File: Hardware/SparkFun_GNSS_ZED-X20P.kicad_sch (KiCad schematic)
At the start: 70 parts, among them J1 USB_C_Receptacle, J10 U.FL, J11 Conn_01x06, J2 Conn_01x06, J3 Conn_01x09, J4 Qwiic_RA, J5 SMA_Edge, J7 Qwiic_RA, J8 JST_Locking_4, J9 I2C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

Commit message: Add panel
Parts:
- added TP2: 1.0mm, SparkFun-Connector:TestPoint-1.0mm, symbol SparkFun-Connector:TestPoint_1.0mm
- L1, L2: value 33nH -> 47nH; symbol SparkFun-Coil:33nH_0603_0.3A -> SparkFun-Coil:47nH_0603_0.3A; Frequency 100MHz -> (none); PROD_ID NDUC-13805 -> NDUC-26402; Resistance (none) -> 0.72
- U5: symbol SparkFun-GPS:ZED-F9P -> SparkFun-GPS:ZED-X20P; PROD_ID IC-16923 -> IC-26061
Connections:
- net 3.3V: now also JP8.2 (B)
- net GEO_STAT: now also D9.1 (K); no longer JP8.2 (B)
- net GND: no longer D9.1 (K)
- net V_BCKP: now also TP2.1
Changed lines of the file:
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@@
 	(wire
 		(pts
+			(xy 260.35 156.21) (xy 260.35 157.48)
+		)
+		(stroke
+			(width 0)
+			(type default)
+		)
+	)
+	(wire
+		(pts
 			(xy 368.3 90.17) (xy 368.3 88.9)
 		)
@@
 		)
 	)
-	(global_label "GEO_STAT"
-		(shape output)
-		(at 269.24 218.44 90)
-		(fields_autoplaced yes)
-		(effects
-			(font
-				(size 1.27 1.27)
-			)
-			(justify left)
-		)
-		(property "Intersheetrefs" "${INTERSHEET_REFS}"
-			(at 269.24 207.1586 90)
-			(effects
-				(font
-					(size 1.27 1.27)
-				)
-				(justify left)
-				(hide yes)
-			)
-		)
-	)
 	(global_label "SDA{slash}~{CS}"
 		(shape bidirectional)
@@
 	)
 	(global_label "RF_IN"
-		(shape input)
+		(shape output)
 		(at 367.03 144.78 90)
 		(fields_autoplaced yes)
@@
 		)
 	)
+	(global_label "GEO_STAT"
+		(shape output)
+		(at 269.24 238.76 270)
+		(fields_autoplaced yes)
+		(effects
+			(font
+				(size 1.27 1.27)
+			)
+			(justify right)
+		)
+		(property "Intersheetrefs" "${INTERSHEET_REFS}"
+			(at 269.24 250.0414 90)
+			(effects
+				(font
+					(size 1.27 1.27)
+				)
+				(justify right)
+				(hide yes)
+			)
+		)
+	)
 	(global_label "RTK_STAT"
 		(shape output)
@@
 	)
 	(global_label "VCC_RF"
-		(shape output)
+		(shape input)
 		(at 389.89 163.83 0)
 		(fields_autoplaced yes)
@@
 	)
 	(symbol
-		(lib_id "SparkFun-Coil:33nH_0603_0.3A")
+		(lib_id "SparkFun-Connector:TestPoint_1.0mm")
+		(at 260.35 156.21 0)
+		(unit 1)
+		(exclude_from_sim no)
+		(in_bom yes)
+		(on_board yes)
+		(dnp no)
+		(fields_autoplaced yes)
+		(property "Reference" "TP2"
+			(at 260.35 151.13 0)
+			(do_not_autoplace yes)
+			(effects
+				(font
+					(size 1.27 1.27)
+				)
+			)
+		)
+		(property "Value" "1.0mm"
+			(at 260.35 160.02 0)
+			(effects
+				(font
+					(size 1.27 1.27)
+				)
+				(hide yes)
+			)
+		)
+		(property "Footprint" "SparkFun-Connector:TestPoint-1.0mm"
+			(at 260.35 162.56 0)
+			(effects
+				(font
+					(size 1.27 1.27)
+				)
+				(hide yes)
+			)
+		)
+		(property "Datasheet" "~"
+			(at 260.35 163.83 0)
+			(effects
+				(font
+					(size 1.27 1.27)
+				)
+				(hide yes)
+			)
+		)
+		(property "Description" "Test Point"
+			(at 260.35 166.37 0)
+			(effects
+				(font
+					(size 1.27 1.27)
+				)
+				(hide yes)
+			)
+		)
+		(pin "1"
+		)
+		(instances
+			(project ""
+				(path "/e3dd3ae4-244d-4cba-9cca-5d2abf83f29a"
+					(reference "TP2")
+					(unit 1)
+				)
+			)
+		)
+	)
+	(symbol
+		(lib_id "SparkFun-Coil:47nH_0603_0.3A")
 		(at 378.46 153.67 90)
 		(mirror x)
@@
 		(fields_autoplaced yes)
 		(property "Reference" "L2"
-			(at 375.92 151.1299 90)
+			(at 375.92 152.3999 90)
 			(effects
 				(font
@@
 			)
 		)
-		(property "Value" "33nH"
-			(at 375.92 153.6699 90)
+		(property "Value" "47nH"
+			(at 375.92 154.9399 90)
 			(effects
 				(font
@@
 			)
 		)
-		(property "Datasheet" "https://www.bourns.com/docs/Product-Datasheets/CI160808.pdf"
+		(property "Datasheet" "https://search.murata.co.jp/Ceramy/image/img/P02/JELF243B-0010.pdf"
 			(at 387.35 153.67 0)
 			(effects
@@
 			)
 		)
-		(property "Description" "Inductor with ferrite core 30 ohm"
-			(at 378.46 153.67 0)
+		(property "Description" "Chip inductor"
+			(at 392.43 153.67 0)
 			(effects
 				(font
@@
 			)
 		)
-		(property "PROD_ID" "NDUC-13805"
+		(property "PROD_ID" "NDUC-26402"
 			(at 384.81 153.67 0)
 			(effects
@@
 			)
 		)
-		(property "Frequency" "100MHz"
-			(at 375.92 156.2099 90)
+		(property "Resistance" "0.72"
+			(at 382.27 153.67 0)
 			(effects
 				(font
 					(size 1.27 1.27)
 				)
-				(justify left)
+				(hide yes)
 			)
 		)
@@
 	(symbol
 		(lib_id "SparkFun-PowerSymbol:3.3V")
+		(at 269.24 218.44 0)
+		(unit 1)
+		(exclude_from_sim no)
+		(in_bom yes)
+		(on_board yes)
+		(dnp no)
+		(property "Reference" "#PWR049"
+			(at 269.24 222.25 0)
+			(effects
+				(font
+					(size 1.27 1.27)
+				)
+				(hide yes)
+			)
+		)
+		(property "Value" "3.3V"
+			(at 269.24 214.63 0)
+			(do_not_autoplace yes)
+			(effects
+				(font
+					(size 1.27 1.27)
+				)
+			)
+		)
+		(property "Footprint" ""
+			(at 269.24 218.44 0)
+			(effects
+				(font
+					(size 1.27 1.27)
+				)
+				(hide yes)
+			)
+		)
+		(property "Datasheet" ""
+			(at 269.24 218.44 0)
+			(effects
+				(font
+					(size 1.27 1.27)
+				)
+				(hide yes)
+			)
+		)
+		(property "Description" "Power symbol creates a global label with name \"3.3V\""
+			(at 269.24 224.79 0)
+			(effects
+				(font
+					(size 1.27 1.27)
+				)
+				(hide yes)
+			)
+		)
+		(pin "1"
+		)
+		(instances
+			(project "SparkFun_GNSS_ZED-X20P"
+				(path "/e3dd3ae4-244d-4cba-9cca-5d2abf83f29a"
+					(reference "#PWR049")
+					(unit 1)
+				)
+			)
+		)
+	)
+	(symbol
+		(lib_id "SparkFun-PowerSymbol:3.3V")
 		(at 179.07 208.28 0)
 		(unit 1)
@@
 	)
 	(symbol
-		(lib_id "SparkFun-PowerSymbol:GND")
-		(at 269.24 238.76 0)
-		(unit 1)
-		(exclude_from_sim no)
-		(in_bom yes)
-		(on_board yes)
-		(dnp no)
-		(property "Reference" "#PWR049"
-			(at 269.24 245.11 0)
-			(effects
-				(font
-					(size 1.27 1.27)
-				)
-				(hide yes)
-			)
-		)
-		(property "Value" "GND"
-			(at 269.24 242.57 0)
-			(effects
-				(font
-					(size 1.27 1.27)
-				)
-			)
-		)
-		(property "Footprint" ""
-			(at 269.24 238.76 0)
-			(effects
-				(font
-					(size 1.27 1.27)
-				)
-				(hide yes)
-			)
-		)
-		(property "Datasheet" ""
-			(at 269.24 238.76 0)
-			(effects
-				(font
-					(size 1.27 1.27)
-				)
-				(hide yes)
-			)
-		)
-		(property "Description" "Power symbol creates a global label with name \"GND\" , ground"
-			(at 269.24 238.76 0)
-			(effects
-				(font
-					(size 1.27 1.27)
-				)
-				(hide yes)
-			)
-		)
-		(pin "1"
-		)
-		(instances
-			(project "SparkFun_GNSS_LG580P"
-				(path "/e3dd3ae4-244d-4cba-9cca-5d2abf83f29a"
-					(reference "#PWR049")
-					(unit 1)
-				)
-			)
-		)
-	)
-	(symbol
 		(lib_id "SparkFun-DiscreteSemi:D_TVS_ESD_4_HS_3.3V")
 		(at 105.41 226.06 0)
@@
 	)
 	(symbol
-		(lib_id "SparkFun-Coil:33nH_0603_0.3A")
+		(lib_id "SparkFun-Coil:47nH_0603_0.3A")
 		(at 355.6 153.67 270)
 		(unit 1)
@@
 		(fields_autoplaced yes)
 		(property "Reference" "L1"
-			(at 358.14 151.1299 90)
+			(at 358.14 152.3999 90)
 			(effects
 				(font
@@
 			)
 		)
-		(property "Value" "33nH"
-			(at 358.14 153.6699 90)
+		(property "Value" "47nH"
+			(at 358.14 154.9399 90)
 			(effects
 				(font
@@
 			)
 		)
-		(property "Datasheet" "https://www.bourns.com/docs/Product-Datasheets/CI160808.pdf"
+		(property "Datasheet" "https://search.murata.co.jp/Ceramy/image/img/P02/JELF243B-0010.pdf"
 			(at 346.71 153.67 0)
 			(effects
@@
 			)
 		)
-		(property "Description" "Inductor with ferrite core 30 ohm"
-			(at 355.6 153.67 0)
+		(property "Description" "Chip inductor"
+			(at 341.63 153.67 0)
 			(effects
 				(font
@@
 			)
 		)
-		(property "PROD_ID" "NDUC-13805"
+		(property "PROD_ID" "NDUC-26402"
 			(at 349.25 153.67 0)
 			(effects
@@
 			)
 		)
-		(property "Frequency" "100MHz"
-			(at 358.14 156.2099 90)
+		(property "Resistance" "0.72"
+			(at 351.79 153.67 0)
 			(effects
 				(font
 					(size 1.27 1.27)
 				)
-				(justify left)
+				(hide yes)
 			)
 		)
@@
 	)
 	(symbol
-		(lib_id "SparkFun-GPS:ZED-F9P")
+		(lib_id "SparkFun-GPS:ZED-X20P")
 		(at 334.01 62.23 0)
 		(unit 1)
@@
 			)
 		)
-		(property "Datasheet" "https://cdn.sparkfun.com/assets/f/8/d/6/d/ZED-F9P-02B_DataSheet_UBX-21023276.pdf"
+		(property "Datasheet" "https://www.u-blox.com/sites/default/files/documents/ZED-X20P_ProductSummary_UBXDOC-304424225-18238.pdf"
 			(at 334.01 95.25 0)
 			(effects
@@
 			)
 		)
-		(property "Description" "u-blox Dual-Band RTK GNSS Receiver"
+		(property "Description" "u-blox All-Band RTK GNSS Receiver"
 			(at 334.01 97.79 0)
 			(effects
@@
 			)
 		)
-		(property "PROD_ID" "IC-16923"
+		(property "PROD_ID" "IC-26061"
 			(at 334.01 92.71 0)
 			(effects
@@
 		(pin "42"
 		)
+		(pin "13"
+		)
+		(pin "16"
+		)
+		(pin "8"
+		)
+		(pin "10"
+		)
+		(pin "11"
+		)
+		(pin "35"
+		)
+		(pin "9"
+		)
+		(pin "15"
+		)
+		(pin "17"
+		)
+		(pin "18"
+		)
+		(pin "21"
+		)
+		(pin "22"
+		)
+		(pin "23"
+		)
+		(pin "24"
+		)
+		(pin "29"
+		)
+		(pin "25"
+		)
+		(pin "30"
+		)
+		(pin "28"
+		)
+		(pin "31"
+		)
+		(pin "54"
+		)
+		(pin "52"
+		)
 		(instances

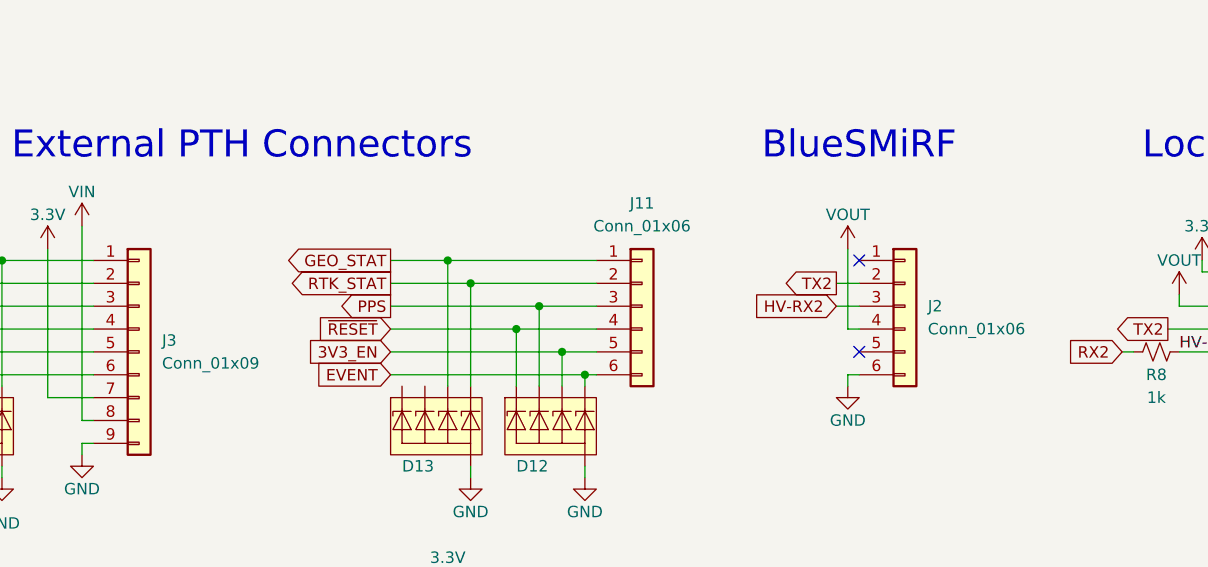
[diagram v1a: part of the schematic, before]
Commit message: Update to new symbol/fp locations
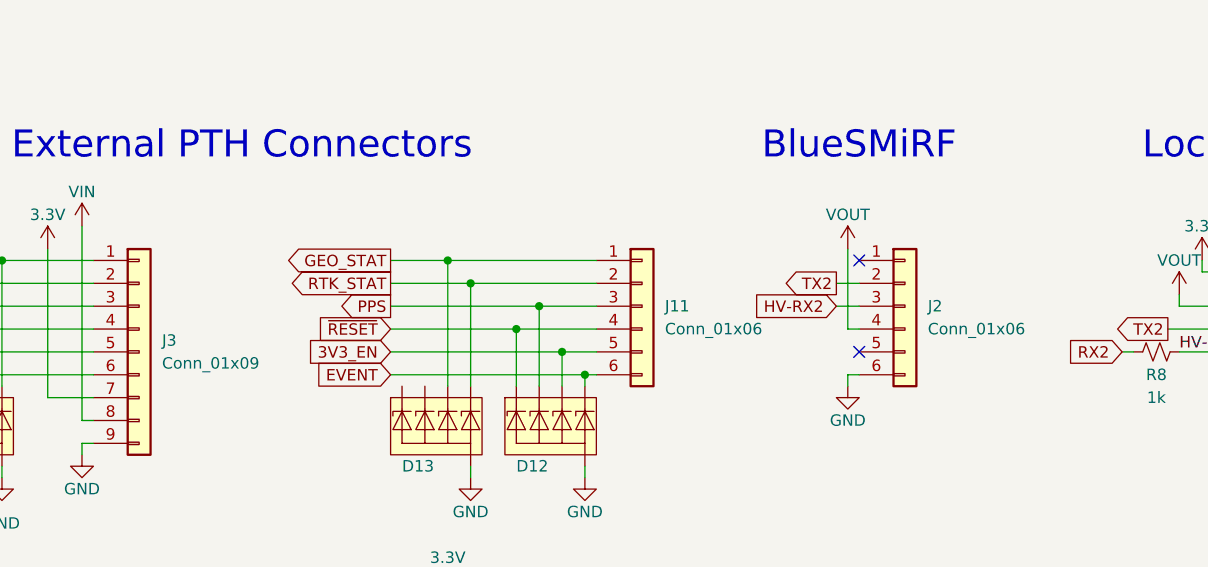
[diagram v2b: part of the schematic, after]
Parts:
- C2: PROD_ID CAP-11015 -> CAP-25001
- J11, J2: footprint SparkFun-Connector:1x06 -> SparkFun-Connector:1x06_P2.54mm; symbol SparkFun-Connector:Conn_01x06 -> SparkFun-Connector:Conn_01x06_P2.54mm
- J3: footprint SparkFun-Connector:1x09 -> SparkFun-Connector:1x09_P2.54mm; symbol SparkFun-Connector:Conn_01x09 -> SparkFun-Connector:Conn_01x09_P2.54mm
- J4, J7: footprint SparkFun-Connector:JST_SMD_1.0mm-4_Black -> SparkFun-Connector:JST_1x04_P1.0mm_Horizontal_SMD; symbol SparkFun-Connector:Qwiic_Right_Angle -> SparkFun-Connector:Qwiic_Horizontal
- J5: footprint SparkFun-Connector:SMA_Edge -> SparkFun-Connector:SMA_Edge_8mm; symbol SparkFun-RF:SMA_EdgeMount -> SparkFun-RF:SMA_EdgeMount_8mm; PROD_ID CONN-08289 -> CONN-19593
- J8: footprint SparkFun-Connector:JST_SMD_1.25mm-4_Locking -> SparkFun-Connector:JST_1x04_P1.25mm_Locking_Horizontal_SMD; symbol SparkFun-Connector:Conn_01x04_JST_1.25mm_Locking -> SparkFun-Connector:Conn_01x04_JST_P1.25mm_Locking_Horizontal_SMD
- J9: footprint SparkFun-Connector:1x04 -> SparkFun-Connector:1x04_P2.54mm; symbol SparkFun-Connector:I2C_01x04 -> SparkFun-Connector:I2CStandard_1x04_P2.54mm
- U5: footprint SparkFun-GPS:ZED-F9P_F9T_F9R_X20P -> SparkFun-GNSS:ZED-F9P_F9T_F9R_X20P; symbol SparkFun-GPS:ZED-X20P -> SparkFun-GNSS:ZED-X20P
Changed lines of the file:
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@@
 	)
 	(symbol
-		(lib_id "SparkFun-RF:SMA_EdgeMount")
+		(lib_id "SparkFun-RF:SMA_EdgeMount_8mm")
 		(at 332.74 148.59 0)
 		(mirror y)
@@
 			)
 		)
-		(property "Footprint" "SparkFun-Connector:SMA_Edge"
+		(property "Footprint" "SparkFun-Connector:SMA_Edge_8mm"
 			(at 332.74 158.75 0)
 			(effects
@@
 			)
 		)
-		(property "Datasheet" "https://www.sparkfun.com/datasheets/Wireless/Antenna/SMA-Connector.pdf"
+		(property "Datasheet" "https://cdn.sparkfun.com/assets/c/2/9/a/7/SMA-KE-347C-H13.5-1.pdf"
 			(at 332.74 161.29 0)
 			(effects
@@
 			)
 		)
-		(property "PROD_ID" "CONN-08289"
+		(property "PROD_ID" "CONN-19593"
 			(at 332.74 156.21 0)
 			(effects
@@
 	)
 	(symbol
-		(lib_id "SparkFun-Connector:Conn_01x04_JST_1.25mm_Locking")
+		(lib_id "SparkFun-Connector:Conn_01x04_JST_P1.25mm_Locking_Horizontal_SMD")
 		(at 189.23 215.9 0)
 		(unit 1)
@@
 			)
 		)
-		(property "Footprint" "SparkFun-Connector:JST_SMD_1.25mm-4_Locking"
+		(property "Footprint" "SparkFun-Connector:JST_1x04_P1.25mm_Locking_Horizontal_SMD"
 			(at 189.23 226.06 0)
 			(effects
@@
 	)
 	(symbol
-		(lib_id "SparkFun-Connector:Conn_01x09")
+		(lib_id "SparkFun-Connector:Conn_01x09_P2.54mm")
 		(at 60.96 218.44 0)
 		(unit 1)
@@
 		(fields_autoplaced yes)
 		(property "Reference" "J3"
-			(at 63.5 217.17 0)
+			(at 63.5 217.1699 0)
 			(effects
 				(font
@@
 		)
 		(property "Value" "Conn_01x09"
-			(at 63.5 219.71 0)
+			(at 63.5 219.7099 0)
 			(effects
 				(font
@@
 			)
 		)
-		(property "Footprint" "SparkFun-Connector:1x09"
-			(at 60.96 218.44 0)
+		(property "Footprint" "SparkFun-Connector:1x09_P2.54mm"
+			(at 60.96 233.68 0)
 			(effects
 				(font
@@
 		)
 		(property "Datasheet" "~"
-			(at 60.96 218.44 0)
+			(at 60.96 236.22 0)
 			(effects
 				(font
@@
 		)
 		(property "Description" "Basic 0.1\" PTH"
-			(at 60.96 218.44 0)
+			(at 60.96 238.76 0)
 			(effects
 				(font
@@
 			)
 		)
-		(property "Datasheet" "https://docs.broadcom.com/docs/AV02-0551EN"
+		(property "Datasheet" "https://www.kingbrightusa.com/images/catalog/SPEC/APT1608SURCK.pdf"
 			(at 238.76 234.95 0)
 			(effects
@@
 	)
 	(symbol
-		(lib_id "SparkFun-Connector:Qwiic_Right_Angle")
+		(lib_id "SparkFun-Connector:Qwiic_Horizontal")
 		(at 68.58 147.32 0)
 		(unit 1)
@@
 			)
 		)
-		(property "Footprint" "SparkFun-Connector:JST_SMD_1.0mm-4_Black"
+		(property "Footprint" "SparkFun-Connector:JST_1x04_P1.0mm_Horizontal_SMD"
 			(at 68.58 160.02 0)
 			(effects
@@
 	)
 	(symbol
-		(lib_id "SparkFun-Connector:I2C_01x04")
+		(lib_id "SparkFun-Connector:I2CStandard_1x04_P2.54mm")
 		(at 101.6 248.92 0)
 		(unit 1)
@@
 			)
 		)
-		(property "Footprint" "SparkFun-Connector:1x04"
+		(property "Footprint" "SparkFun-Connector:1x04_P2.54mm"
 			(at 101.6 260.35 0)
 			(effects
@@
 		)
 		(property "Datasheet" "~"
-			(at 104.14 248.92 0)
+			(at 101.6 265.43 0)
 			(effects
 				(font
@@
 			)
 		)
-		(property "Description" "Coomon 4 pin PTH connector for I2C"
+		(property "Description" "Common 4 pin PTH connector for I2C"
 			(at 101.6 262.89 0)
 			(effects
@@
 	)
 	(symbol
-		(lib_id "SparkFun-GPS:ZED-X20P")
+		(lib_id "SparkFun-GNSS:ZED-X20P")
 		(at 334.01 62.23 0)
 		(unit 1)
@@
 			)
 		)
-		(property "Footprint" "SparkFun-GPS:ZED-F9P_F9T_F9R_X20P"
+		(property "Footprint" "SparkFun-GNSS:ZED-F9P_F9T_F9R_X20P"
 			(at 334.01 90.17 0)
 			(effects
@@
 	)
 	(symbol
-		(lib_id "SparkFun-Connector:Conn_01x06")
+		(lib_id "SparkFun-Connector:Conn_01x06_P2.54mm")
 		(at 146.05 213.36 0)
 		(unit 1)
@@
 		(fields_autoplaced yes)
 		(property "Reference" "J2"
-			(at 148.59 213.36 0)
+			(at 148.59 213.3599 0)
 			(effects
 				(font
@@
 		)
 		(property "Value" "Conn_01x06"
-			(at 148.59 215.9 0)
+			(at 148.59 215.8999 0)
 			(effects
 				(font
@@
 			)
 		)
-		(property "Footprint" "SparkFun-Connector:1x06"
-			(at 146.05 213.36 0)
+		(property "Footprint" "SparkFun-Connector:1x06_P2.54mm"
+			(at 146.05 226.06 0)
 			(effects
 				(font
@@
 		)
 		(property "Datasheet" "~"
-			(at 146.05 213.36 0)
+			(at 146.05 228.6 0)
 			(effects
 				(font
@@
 		)
 		(property "Description" "Basic 0.1\" PTH"
-			(at 146.05 213.36 0)
+			(at 146.05 231.14 0)
 			(effects
 				(font
@@
 	)
 	(symbol
-		(lib_id "SparkFun-Connector:Qwiic_Right_Angle")
+		(lib_id "SparkFun-Connector:Qwiic_Horizontal")
 		(at 102.87 147.32 0)
 		(unit 1)
@@
 			)
 		)
-		(property "Footprint" "SparkFun-Connector:JST_SMD_1.0mm-4_Black"
+		(property "Footprint" "SparkFun-Connector:JST_1x04_P1.0mm_Horizontal_SMD"
 			(at 102.87 160.02 0)
 			(effects
@@
 	)
 	(symbol
-		(lib_id "SparkFun-Connector:Conn_01x06")
+		(lib_id "SparkFun-Connector:Conn_01x06_P2.54mm")
 		(at 116.84 213.36 0)
 		(unit 1)
@@
 		(fields_autoplaced yes)
 		(property "Reference" "J11"
-			(at 116.84 201.93 0)
+			(at 119.38 213.3599 0)
 			(effects
 				(font
 					(size 1.27 1.27)
 				)
+				(justify left)
 			)
 		)
 		(property "Value" "Conn_01x06"
-			(at 116.84 204.47 0)
+			(at 119.38 215.8999 0)
 			(effects
 				(font
 					(size 1.27 1.27)
 				)
+				(justify left)
 			)
 		)
-		(property "Footprint" "SparkFun-Connector:1x06"
-			(at 116.84 213.36 0)
+		(property "Footprint" "SparkFun-Connector:1x06_P2.54mm"
+			(at 116.84 226.06 0)
 			(effects
 				(font
@@
 		)
 		(property "Datasheet" "~"
-			(at 116.84 213.36 0)
+			(at 116.84 228.6 0)
 			(effects
 				(font
@@
 		)
 		(property "Description" "Basic 0.1\" PTH"
-			(at 116.84 213.36 0)
+			(at 116.84 231.14 0)
 			(effects
 				(font
@@
 			)
 		)
-		(property "PROD_ID" "CAP-11015"
+		(property "PROD_ID" "CAP-25001"
 			(at 220.98 86.36 0)
 			(effects
